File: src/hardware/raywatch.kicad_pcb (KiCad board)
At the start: 2 copper layers, 17.1 x 39.2 mm, 387 parts, among them J1 Conn_02x05_Odd_Even, J10 Conn_01x04_Pin, J11 Conn_01x04_Pin, J12 Conn_01x02_Pin, J13 Conn_01x02_Pin, J14 Conn_02x08_Top_Bottom, J15 Conn_02x08_Top_Bottom, J16 Conn_02x08_Top_Bottom, J17 Conn_02x08_Top_Bottom, J18 Conn_01x02_Pin, J19 Conn_01x02_Pin, J2 Conn_01x02_Pin, J20 Conn_01x02_Pin, J21 Conn_02x08_Top_Bottom, J22 Conn_01x02_Pin, J23 Conn_01x04_Pin, J24 Conn_01x02_Pin, J25 Conn_01x02_Pin, J26 Conn_01x02_Pin, J27 Conn_01x02_Pin, J28 Conn_01x04_Pin, J29 Conn_01x04_Pin, J3 Conn_01x02_Pin, J30 Conn_01x02_Pin, J31 Conn_01x02_Pin, J32 046809612110846+, J33 Conn_01x02_Pin, J34 Conn_01x02_Pin, J35 Conn_01x02_Pin, J36 Conn_01x02_Pin, J37 Conn_01x02_Pin, J38 Conn_01x02_Pin, J39 Conn_01x02_Pin, J4 Conn_01x02_Pin, J40 Conn_01x02_Pin, J41 Conn_01x02_Pin, J42 Conn_01x02_Pin, J43 Conn_01x02_Pin, J44 Conn_01x02_Pin, J45 Conn_01x02_Pin, J46 Conn_01x02_Pin, J47 Conn_01x02_Pin, J48 Conn_01x04_Pin, J49 MSD-1-A, J5 Conn_01x02_Pin, J50 Conn_01x02_Pin, J51 Conn_01x02_Pin, J52 Conn_01x01_Pin, J53 Conn_01x02_Pin, J54 Conn_01x02_Pin, J55 Conn_01x02_Pin, J56 Conn_01x02_Pin, J57 Conn_01x02_Pin, J58 Conn_01x02_Pin, J59 Conn_01x02_Pin, J6 Conn_01x04_Pin, J60 Conn_01x01_Pin, J61 Conn_01x02_Pin, J62 Conn_01x02_Pin, J63 Conn_01x04_Pin, J64 Conn_01x04_Pin, J65 Conn_01x02_Pin, J66 Conn_01x02_Pin, J67 Conn_01x02_Pin, J68 Conn_02x08_Top_Bottom, J69 Conn_01x02_Pin, J7 Conn_01x04_Pin, J70 Conn_01x01_Pin, J71 Conn_02x08_Top_Bottom, J72 Conn_01x02_Pin, J73 Conn_02x08_Top_Bottom, J74 BM29B0.6-2DS/2-0.35V51, J75 Conn_01x02_Pin, J76 Conn_01x02_Pin, J77 Conn_01x02_Pin, J78 Conn_01x02_Pin, J79 Conn_01x04_Pin, J8 Conn_01x04_Pin, J80 Conn_01x02_Pin, J81 Conn_01x04_Pin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

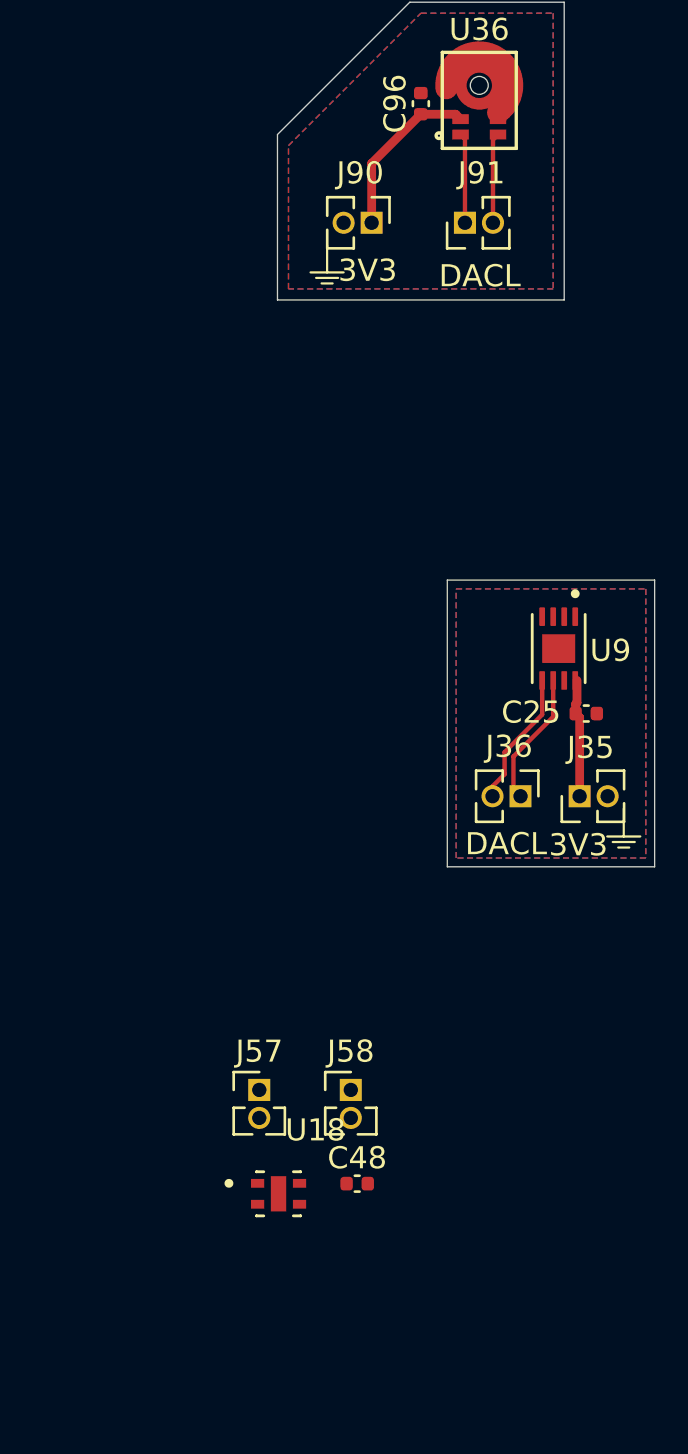
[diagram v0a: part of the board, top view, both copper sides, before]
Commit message: Rounded tracks
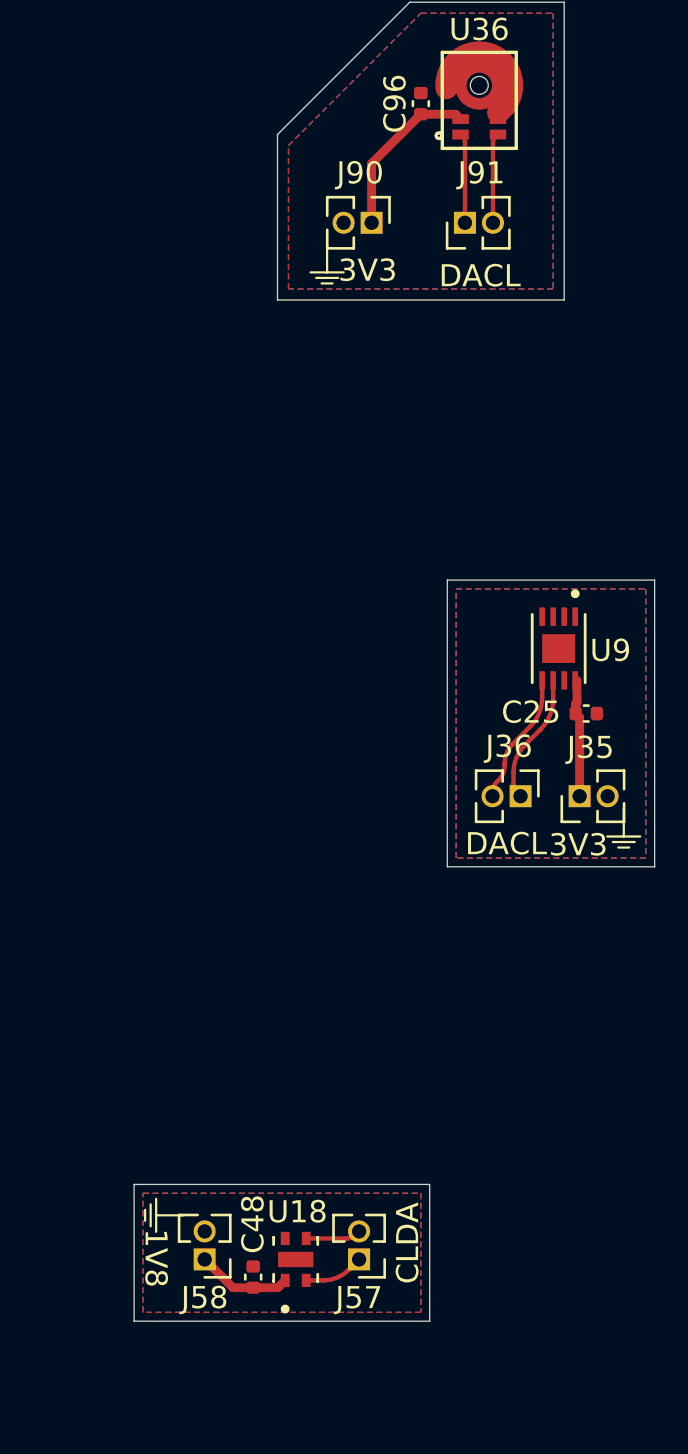
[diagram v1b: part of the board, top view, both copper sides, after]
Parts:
- moved J58 10.1 mm to (239.2, 80.0), turned to 180 degrees
- moved J57 8.92 mm to (246.2, 80.0), turned to 180 degrees
- moved C48 6.34 mm to (241.4, 80.8), turned to 90 degrees
- moved U18 3.07 mm to (243.3, 80.0), turned to 90 degrees
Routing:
- net +1V8: track 0.00 -> 4.32 mm
- net /Humidity/SCL1V8: track 0.00 -> 2.72 mm
- net /Humidity/SDA1V8: track 0.00 -> 2.51 mm
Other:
- board size 17.1 x 39.2 mm -> 23.6 x 59.8 mm
- board text added: "1V8"

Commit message: Applied fixes
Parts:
- J14, J15, J16, J17, J21, J68, J71, J73, J82, J83: value Conn_02x08_Top_Bottom -> Conn_02x08_Odd_Even
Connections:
- J14 pad 11: /MC: Microcontroller/SCL2 -> /MC: Microcontroller/SDA2
- J14 pad 13: /MC: Microcontroller/SCL2 -> /MC: Microcontroller/SDA2
- J14 pad 15: /MC: Microcontroller/SCL2 -> /MC: Microcontroller/SDA2
- J14 pad 2: /MC: Microcontroller/SDA2 -> /MC: Microcontroller/SCL2
- J14 pad 4: /MC: Microcontroller/SDA2 -> /MC: Microcontroller/SCL2
- J14 pad 6: /MC: Microcontroller/SDA2 -> /MC: Microcontroller/SCL2
- J14 pad 8: /MC: Microcontroller/SDA2 -> /MC: Microcontroller/SCL2
- J14 pad 9: /MC: Microcontroller/SCL2 -> /MC: Microcontroller/SDA2
- J15 pad 11: /MC: Microcontroller/SCL -> /MC: Microcontroller/SDA
- J15 pad 13: /MC: Microcontroller/SCL -> /MC: Microcontroller/SDA
- J15 pad 15: /MC: Microcontroller/SCL -> /MC: Microcontroller/SDA
- J15 pad 2: /MC: Microcontroller/SDA -> /MC: Microcontroller/SCL
- J15 pad 4: /MC: Microcontroller/SDA -> /MC: Microcontroller/SCL
- J15 pad 6: /MC: Microcontroller/SDA -> /MC: Microcontroller/SCL
- J15 pad 8: /MC: Microcontroller/SDA -> /MC: Microcontroller/SCL
- J15 pad 9: /MC: Microcontroller/SCL -> /MC: Microcontroller/SDA
- J16 pad 11: /MC: Microcontroller/SCL1V8 -> /MC: Microcontroller/SDA1V8
- J16 pad 13: /MC: Microcontroller/SCL1V8 -> /MC: Microcontroller/SDA1V8
- J16 pad 15: /MC: Microcontroller/SCL1V8 -> /MC: Microcontroller/SDA1V8
- J16 pad 2: /MC: Microcontroller/SDA1V8 -> /MC: Microcontroller/SCL1V8
- J16 pad 4: /MC: Microcontroller/SDA1V8 -> /MC: Microcontroller/SCL1V8
- J16 pad 6: /MC: Microcontroller/SDA1V8 -> /MC: Microcontroller/SCL1V8
- J16 pad 8: /MC: Microcontroller/SDA1V8 -> /MC: Microcontroller/SCL1V8
- J16 pad 9: /MC: Microcontroller/SCL1V8 -> /MC: Microcontroller/SDA1V8
- J68 pad 11: GND -> +1V8
- J68 pad 13: GND -> +1V8
- J68 pad 15: GND -> +1V8
- J68 pad 2: +1V8 -> GND
- J68 pad 4: +1V8 -> GND
- J68 pad 6: +1V8 -> GND
- J68 pad 8: +1V8 -> GND
- J68 pad 9: GND -> +1V8
- J71 pad 11: GND -> +3V0
- J71 pad 13: GND -> +3V0
- J71 pad 15: GND -> +3V0
- J71 pad 2: +3V0 -> GND
- J71 pad 4: +3V0 -> GND
- J71 pad 6: +3V0 -> GND
- J71 pad 8: +3V0 -> GND
- J71 pad 9: GND -> +3V0
- J73 pad 11: GND -> +3V3
- J73 pad 13: GND -> +3V3
- J73 pad 15: GND -> +3V3
- J73 pad 2: +3V3 -> GND
- J73 pad 4: +3V3 -> GND
- J73 pad 6: +3V3 -> GND
- J73 pad 8: +3V3 -> GND
- J73 pad 9: GND -> +3V3
- J82 pad 11: GND -> +4V5
- J82 pad 13: GND -> +4V5
- J82 pad 15: GND -> +4V5
- J82 pad 2: +4V5 -> GND
- J82 pad 4: +4V5 -> GND
- J82 pad 6: +4V5 -> GND
- J82 pad 8: +4V5 -> GND
- J82 pad 9: GND -> +4V5
- J83 pad 11: GND -> +4V5
- J83 pad 13: GND -> +4V5
- J83 pad 15: GND -> +4V5
- J83 pad 2: +4V5 -> GND
- J83 pad 4: +4V5 -> GND
- J83 pad 6: +4V5 -> GND
- J83 pad 8: +4V5 -> GND
- J83 pad 9: GND -> +4V5
- U3 pad 1: Net-(J17-Pin_9) -> Net-(J17-Pin_1)
- U3 pad 10: Net-(J17-Pin_1) -> Net-(J17-Pin_2)
- U3 pad 11: Net-(J17-Pin_2) -> Net-(J17-Pin_4)
- U3 pad 12: Net-(J17-Pin_3) -> Net-(J17-Pin_6)
- U3 pad 13: Net-(J17-Pin_4) -> Net-(J17-Pin_8)
- U3 pad 14: Net-(J17-Pin_5) -> Net-(J17-Pin_10)
- U3 pad 15: Net-(J17-Pin_6) -> Net-(J17-Pin_12)
- U3 pad 16: Net-(J17-Pin_7) -> Net-(J17-Pin_14)
- U3 pad 17: Net-(J17-Pin_8) -> Net-(J17-Pin_16)
- U3 pad 2: Net-(J17-Pin_10) -> Net-(J17-Pin_3)
- U3 pad 3: Net-(J17-Pin_11) -> Net-(J17-Pin_5)
- U3 pad 4: Net-(J17-Pin_12) -> Net-(J17-Pin_7)
- U3 pad 5: Net-(J17-Pin_13) -> Net-(J17-Pin_9)
- U3 pad 6: Net-(J17-Pin_14) -> Net-(J17-Pin_11)
- U3 pad 7: Net-(J17-Pin_15) -> Net-(J17-Pin_13)
- U3 pad 8: Net-(J17-Pin_16) -> Net-(J17-Pin_15)
- U4 pad 1: Net-(J21-Pin_9) -> Net-(J21-Pin_1)
- U4 pad 10: Net-(J21-Pin_1) -> Net-(J21-Pin_2)
- U4 pad 11: Net-(J21-Pin_2) -> Net-(J21-Pin_4)
- U4 pad 12: Net-(J21-Pin_3) -> Net-(J21-Pin_6)
- U4 pad 13: Net-(J21-Pin_4) -> Net-(J21-Pin_8)
- U4 pad 14: Net-(J21-Pin_5) -> Net-(J21-Pin_10)
- U4 pad 15: Net-(J21-Pin_6) -> Net-(J21-Pin_12)
- U4 pad 16: Net-(J21-Pin_7) -> Net-(J21-Pin_14)
- U4 pad 17: Net-(J21-Pin_8) -> Net-(J21-Pin_16)
- U4 pad 2: Net-(J21-Pin_10) -> Net-(J21-Pin_3)
- U4 pad 3: Net-(J21-Pin_11) -> Net-(J21-Pin_5)
- U4 pad 4: Net-(J21-Pin_12) -> Net-(J21-Pin_7)
- U4 pad 5: Net-(J21-Pin_13) -> Net-(J21-Pin_9)
- U4 pad 6: Net-(J21-Pin_14) -> Net-(J21-Pin_11)
- U4 pad 7: Net-(J21-Pin_15) -> Net-(J21-Pin_13)
- U4 pad 8: Net-(J21-Pin_16) -> Net-(J21-Pin_15)

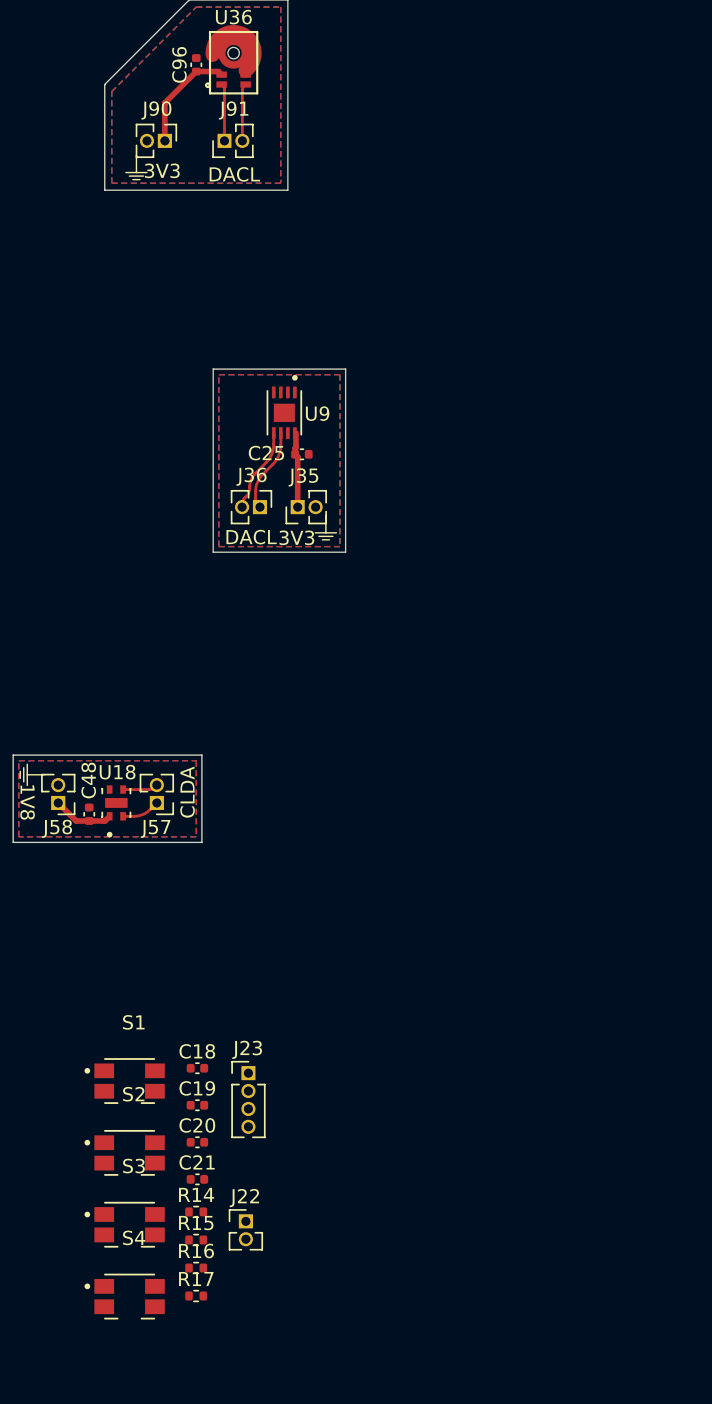
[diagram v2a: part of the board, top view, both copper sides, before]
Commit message: Added Buttons
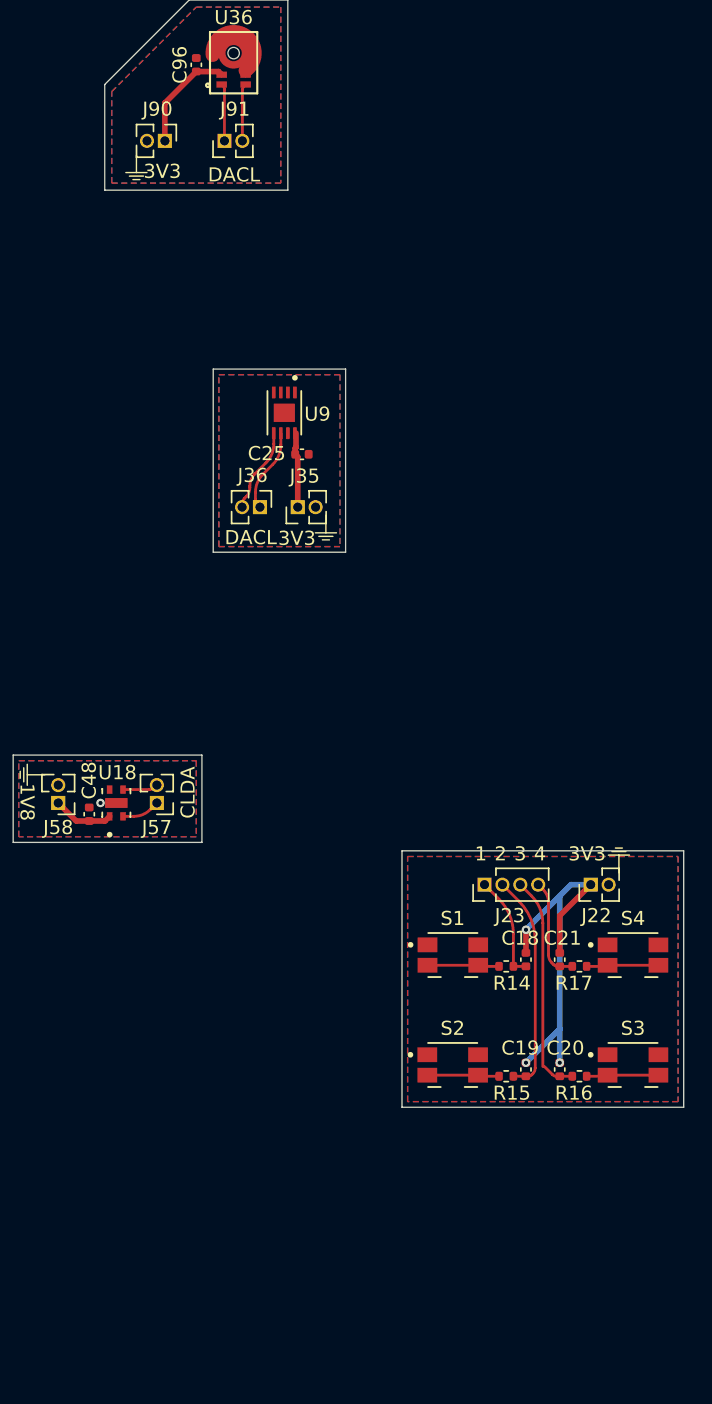
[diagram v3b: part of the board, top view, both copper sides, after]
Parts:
- moved S4 43.2 mm to (280.0, 90.8)
- moved S3 37.5 mm to (280.0, 98.6)
- moved R17 35.9 mm to (276.2, 91.6), turned to 180 degrees
- moved J22 34.2 mm to (277.0, 85.8), turned to 90 degrees
- moved R16 30.4 mm to (276.2, 99.4), turned to 180 degrees
- moved C21 30.1 mm to (274.8, 91.1), turned to 90 degrees
- moved R14 28.1 mm to (271.0, 91.6)
- moved C20 26.2 mm to (274.8, 98.9), turned to 90 degrees
- moved R15 24.9 mm to (271.0, 99.4)
- moved S1 24.6 mm to (267.2, 90.8)
- moved C18 24.6 mm to (272.4, 91.1), turned to 90 degrees
- moved S2 23.8 mm to (267.2, 98.6)
- moved C19 23.5 mm to (272.4, 98.9), turned to 90 degrees
- moved J23 21.4 mm to (269.5, 85.8), turned to 90 degrees
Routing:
- net +3V3: track 13.1 -> 41.7 mm, vias 0 -> 3
- net /Buttons/BTN3: track 0.00 -> 15.7 mm
- net /Buttons/BTN2: track 0.00 -> 15.7 mm
- net /Buttons/BTN1: track 0.00 -> 7.55 mm
- net /Buttons/BTN4: track 0.00 -> 7.49 mm
- net Net-(R16-Pad1): track 0.00 -> 5.11 mm
- net Net-(R17-Pad1): track 0.00 -> 5.11 mm
- net Net-(R15-Pad1): track 0.00 -> 5.11 mm
- net Net-(R14-Pad1): track 0.00 -> 5.10 mm
- net GND: vias 0 -> 1
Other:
- board size 23.6 x 59.8 mm -> 47.6 x 78.6 mm
- board text added: "1"
- board text added: "2"
- board text added: "3"
- board text added: "4"

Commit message: Added Light Sensor PCB
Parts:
- moved U24 103.5 mm to (272.8, 63.7)
- moved C60 100.6 mm to (271.0, 63.7), turned to -90 degrees
- moved J66 95.9 mm to (275.7, 67.3), turned to -90 degrees
- moved J65 95.1 mm to (269.9, 67.3), turned to 90 degrees
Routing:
- net /Light Sensor/SCL: track 0.00 -> 4.94 mm
- net /Light Sensor/SDA: track 0.00 -> 3.59 mm
- net +3V3: track 41.7 -> 42.8 mm
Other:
- outline, holes or cut-outs redrawn
